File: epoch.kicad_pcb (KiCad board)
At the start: 4 copper layers, 28 x 34 mm, 33 parts, among them J1 USB_OTG, J2 CONN_01X05, P3 CONN_01X10, SW1 SW_Reset, SW2 SW_Up, SW3 SW_Middle, SW4 SW_Down, U1 MIC5219-3.3BM5, U2 ATSAMD21Ennc-AU, U3 DS3231MZ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

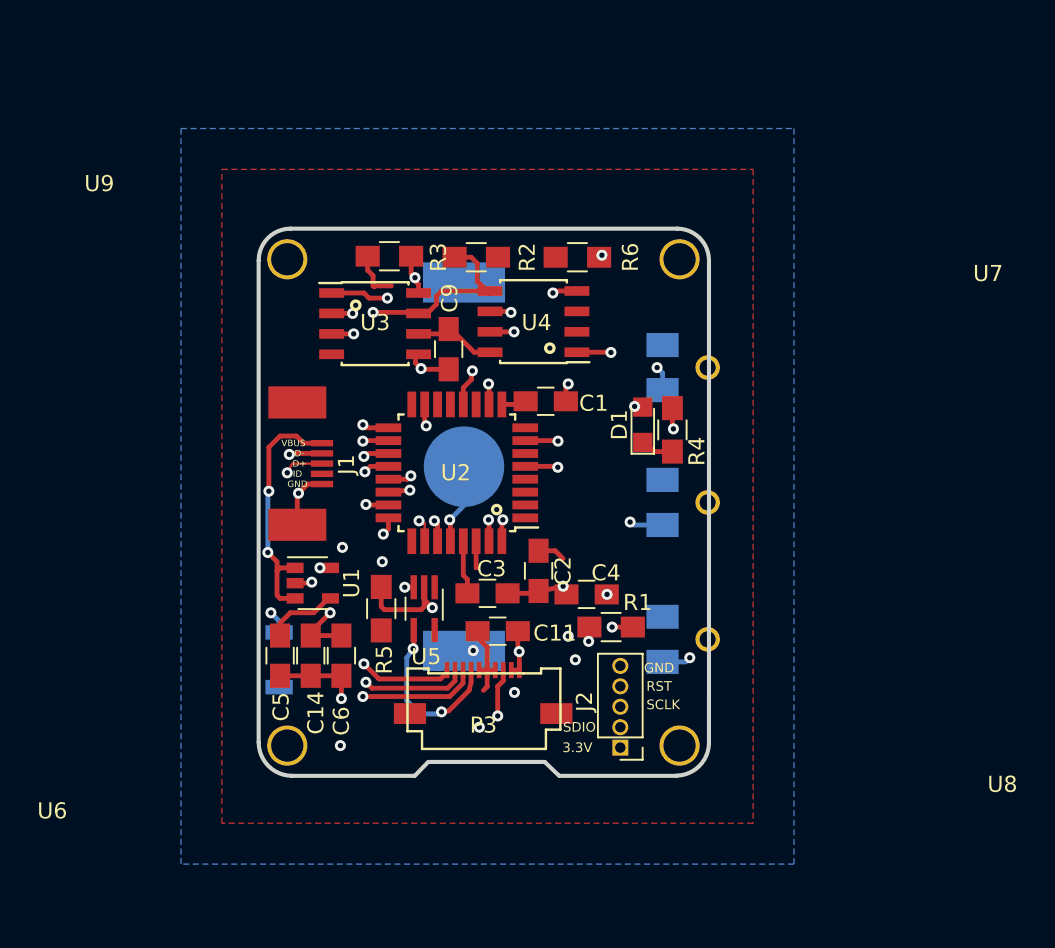
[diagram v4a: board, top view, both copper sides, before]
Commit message: Increase drill size to 2.1.  Rework daughter board
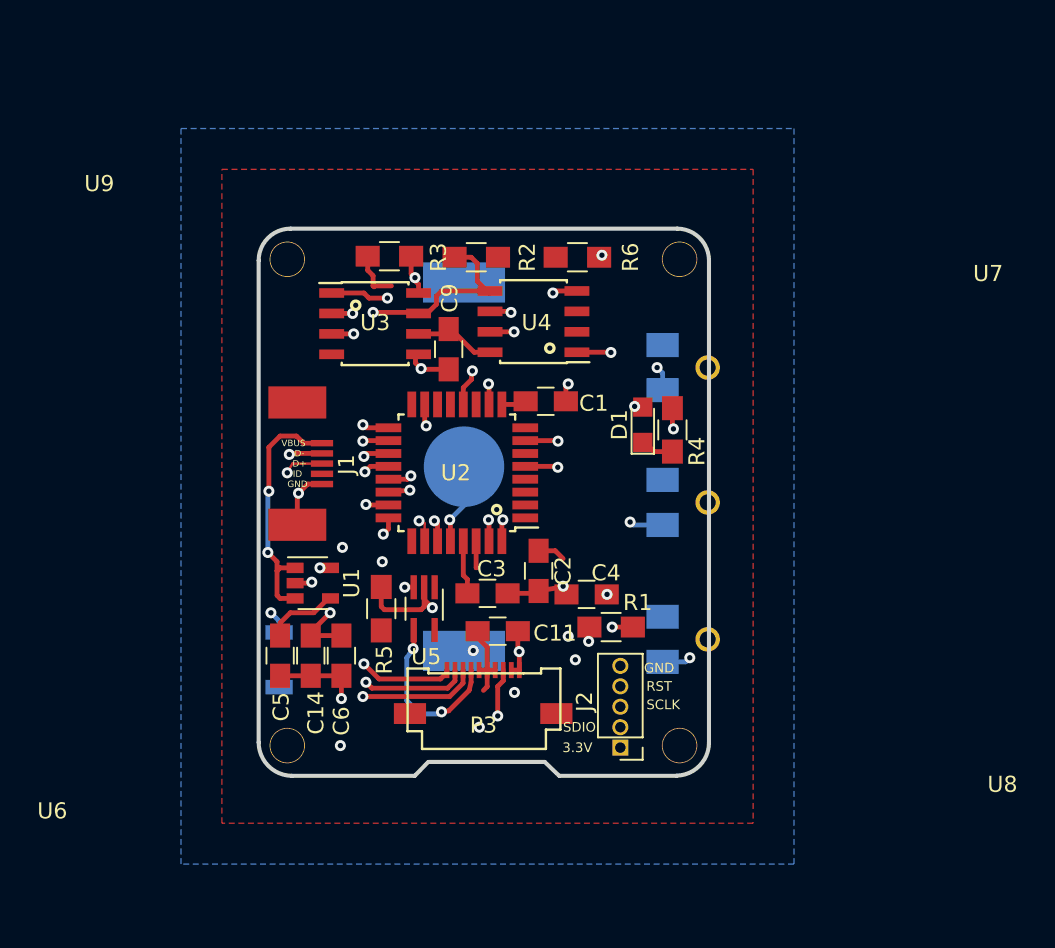
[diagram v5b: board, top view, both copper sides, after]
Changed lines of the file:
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@@
     (1 In1.Cu signal)
     (2 In2.Cu signal)
-    (31 B.Cu signal hide)
+    (31 B.Cu signal)
     (34 B.Paste user)
     (35 F.Paste user)
@@
   )
   (setup
-    (last_trace_width 0.3)
+    (last_trace_width 0.1524)
     (user_trace_width 0.1524)
     (user_trace_width 0.2)
@@
     (mod_text_size 1 1)
     (mod_text_width 0.15)
-    (pad_size 2.5 2.5)
-    (pad_drill 2)
+    (pad_size 2.2 2.2)
+    (pad_drill 2.1)
     (pad_to_mask_clearance 0)
     (aux_axis_origin 0 0)
@@
       (effects (font (size 1 1) (thickness 0.15)))
     )
-    (pad 1 thru_hole circle (at 0 0) (size 2.5 2.5) (drill 2) (layers *.Cu *.Mask))
+    (pad 1 thru_hole circle (at 0 0) (size 2.2 2.2) (drill 2.1) (layers *.Cu *.Mask))
   )
   (module my-fp-library:MH2mm (layer F.Cu)
@@
       (effects (font (size 1 1) (thickness 0.15)))
     )
-    (pad 1 thru_hole circle (at 0.127 0) (size 2.5 2.5) (drill 2) (layers *.Cu *.Mask))
+    (pad 1 thru_hole circle (at 0.127 0) (size 2.2 2.2) (drill 2.1) (layers *.Cu *.Mask))
   )
   (module my-fp-library:MH2mm (layer F.Cu)
@@
       (effects (font (size 1 1) (thickness 0.15)))
     )
-    (pad 1 thru_hole circle (at 0 -0.127) (size 2.5 2.5) (drill 2) (layers *.Cu *.Mask))
+    (pad 1 thru_hole circle (at 0 -0.127) (size 2.2 2.2) (drill 2.1) (layers *.Cu *.Mask))
   )
   (module my-fp-library:MH2mm (layer F.Cu)
@@
       (effects (font (size 1 1) (thickness 0.15)))
     )
-    (pad 1 thru_hole circle (at -0.127 0.254) (size 2.5 2.5) (drill 2) (layers *.Cu *.Mask))
+    (pad 1 thru_hole circle (at -0.127 0.254) (size 2.2 2.2) (drill 2.1) (layers *.Cu *.Mask))
   )
   (module LEDs:LED_0805 (layer F.Cu)

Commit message: V2.0 - Manufactured Board and Adapter
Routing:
- net 32KHz: track 44.6 -> 28.4 mm
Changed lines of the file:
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@@
     (links 80)
     (no_connects 1)
-    (area 101.218844 54.355999 129.463801 88.620601)
+    (area 82.8926 44.9196 152.154639 97.2934)
     (thickness 1.6002)
     (drawings 20)
-    (tracks 431)
+    (tracks 430)
     (zones 0)
     (modules 33)
@@
   (segment (start 123.2408 56.9468) (end 122.682 56.134) (width 0.3) (layer In2.Cu) (net 24))
   (segment (start 123.2408 62.1792) (end 123.2408 56.9468) (width 0.3) (layer In2.Cu) (net 24))
-  (segment (start 107.0356 62.1792) (end 123.2408 62.1792) (width 0.3) (layer In2.Cu) (net 24))
   (via (at 123.2408 62.1792) (size 0.6858) (drill 0.3302) (layers F.Cu B.Cu) (net 24))
   (segment (start 109.347 58.801) (end 109.347 57.15) (width 0.3) (layer In2.Cu) (net 24))

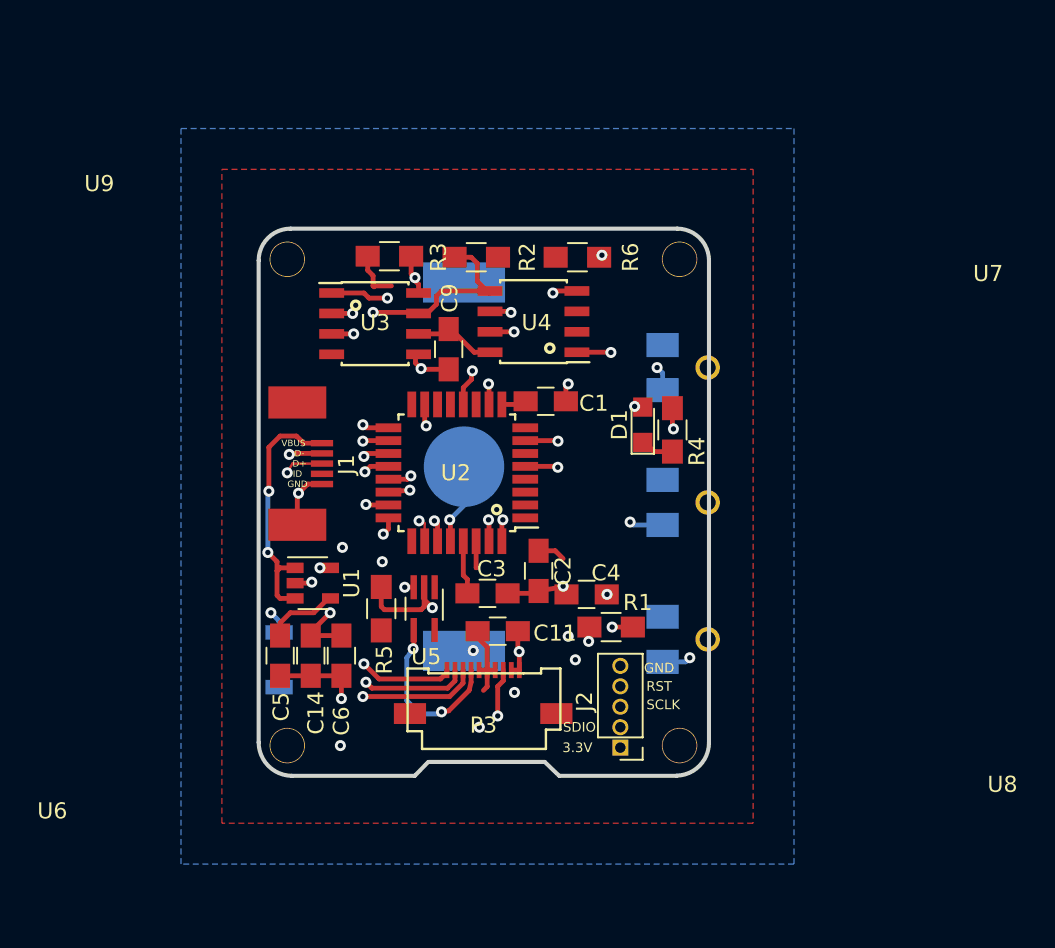
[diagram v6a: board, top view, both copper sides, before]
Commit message: update for RTC battery grounding and clock pull-up increased to 1M to reduce power consumption
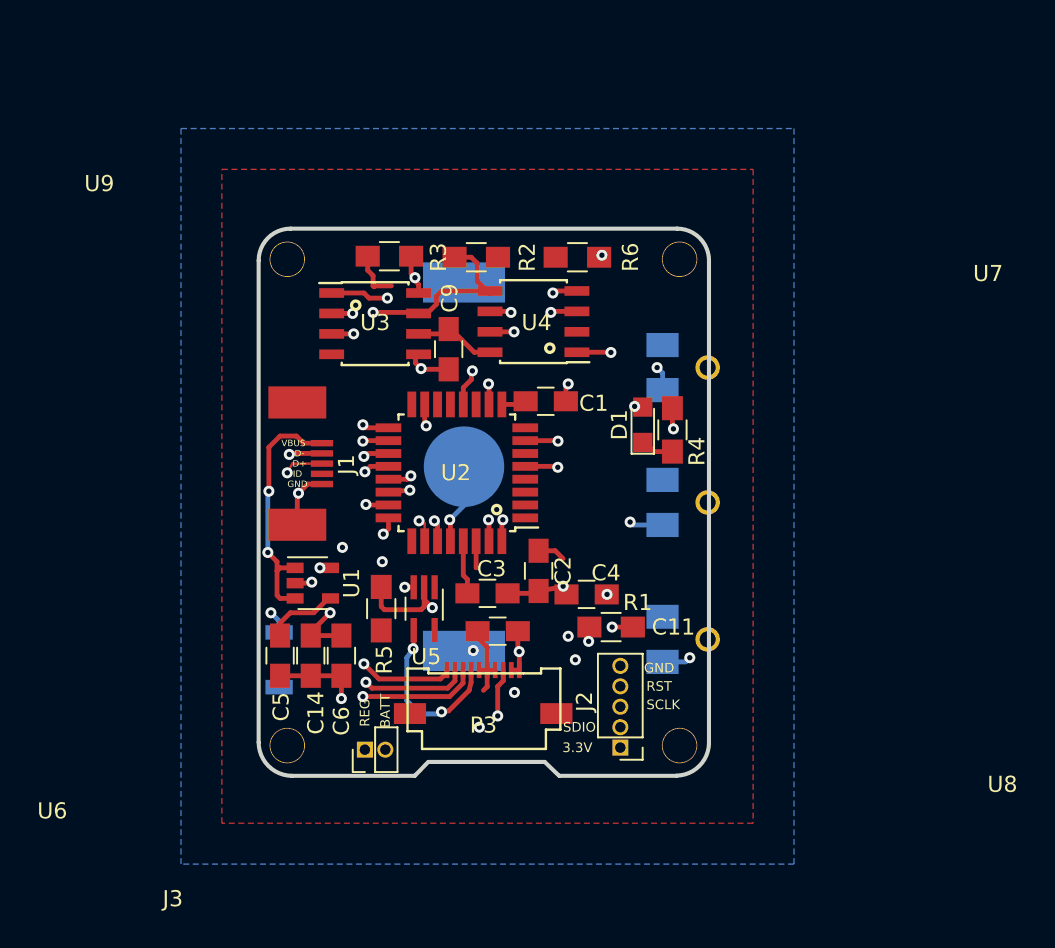
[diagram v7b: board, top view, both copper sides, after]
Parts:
- added J3: CONN_01X02, Pin_Headers:Pin_Header_Straight_1x02_Pitch1.27mm, F.Cu at (108.0, 86.9)
- R6: value 10K -> 1M
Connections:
- BT1 pad 1: SWDCLK/+3.3V(BATT) -> +3.3V(BATT)
- C14 pad 1: SWDIO/+3.3V(REGUL) -> +3.3V(REGUL)
- C6 pad 1: SWDIO/+3.3V(REGUL) -> +3.3V(REGUL)
- J2 pad 2: SWDIO/+3.3V(REGUL) -> SWDIO
- J2 pad 3: SWDCLK/+3.3V(BATT) -> SWDCLK
- U1 pad 5: SWDIO/+3.3V(REGUL) -> +3.3V(REGUL)
- U2 pad 31: SWDCLK/+3.3V(BATT) -> SWDCLK
- U2 pad 32: SWDIO/+3.3V(REGUL) -> SWDIO
- U4 pad 3: (no net) -> (GND)
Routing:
- net SWDIO/+3.3V(REGUL): track 50.4 -> 0.00 mm, vias 5 -> 0
- net SWDCLK/+3.3V(BATT): track 26.8 -> 0.00 mm, vias 2 -> 0
- net SWDIO: track 0.00 -> 21.0 mm, vias 0 -> 2
- net SWDCLK: track 0.00 -> 20.4 mm, vias 0 -> 1
- net +3.3V(REGUL): track 0.00 -> 18.8 mm, vias 0 -> 2
- net +3.3V(BATT): track 0.00 -> 14.8 mm, vias 0 -> 1
- net (GND): track 31.4 -> 33.1 mm, vias 13 -> 14
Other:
- board text added: "BATT"
- board text added: "REG"

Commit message: V3
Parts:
- J1: moved to B.Cu
- moved J1 6.36 mm to (104.3, 62.7), turned to 90 degrees
- moved C1 0.85 mm to (120.0, 65.4)
- moved BT1 0.65 mm to (114.7, 69.6)
- moved U2 0.51 mm to (114.2, 69.7)
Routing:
- net USB_D+: track 13.2 -> 18.9 mm
- net USB_D-: track 11.9 -> 16.2 mm
- net (+3.3): track 18.4 -> 22.4 mm
- net (GND): track 33.1 -> 36.2 mm, vias 14 -> 13
- net VCC: track 15.6 -> 18.6 mm, vias 2 -> 1
- net SPI_CS: track 25.9 -> 26.9 mm
- net +3.3V(BATT): track 14.8 -> 13.8 mm
- net RESET: track 46.0 -> 46.6 mm
